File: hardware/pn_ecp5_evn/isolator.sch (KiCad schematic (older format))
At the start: 14 parts, among them U901 ADS7868, U902 ADS7868, U903 Si8640BB-B-IU, U904 Si8640BB-B-IU, U905 Si8642BB-B-IU

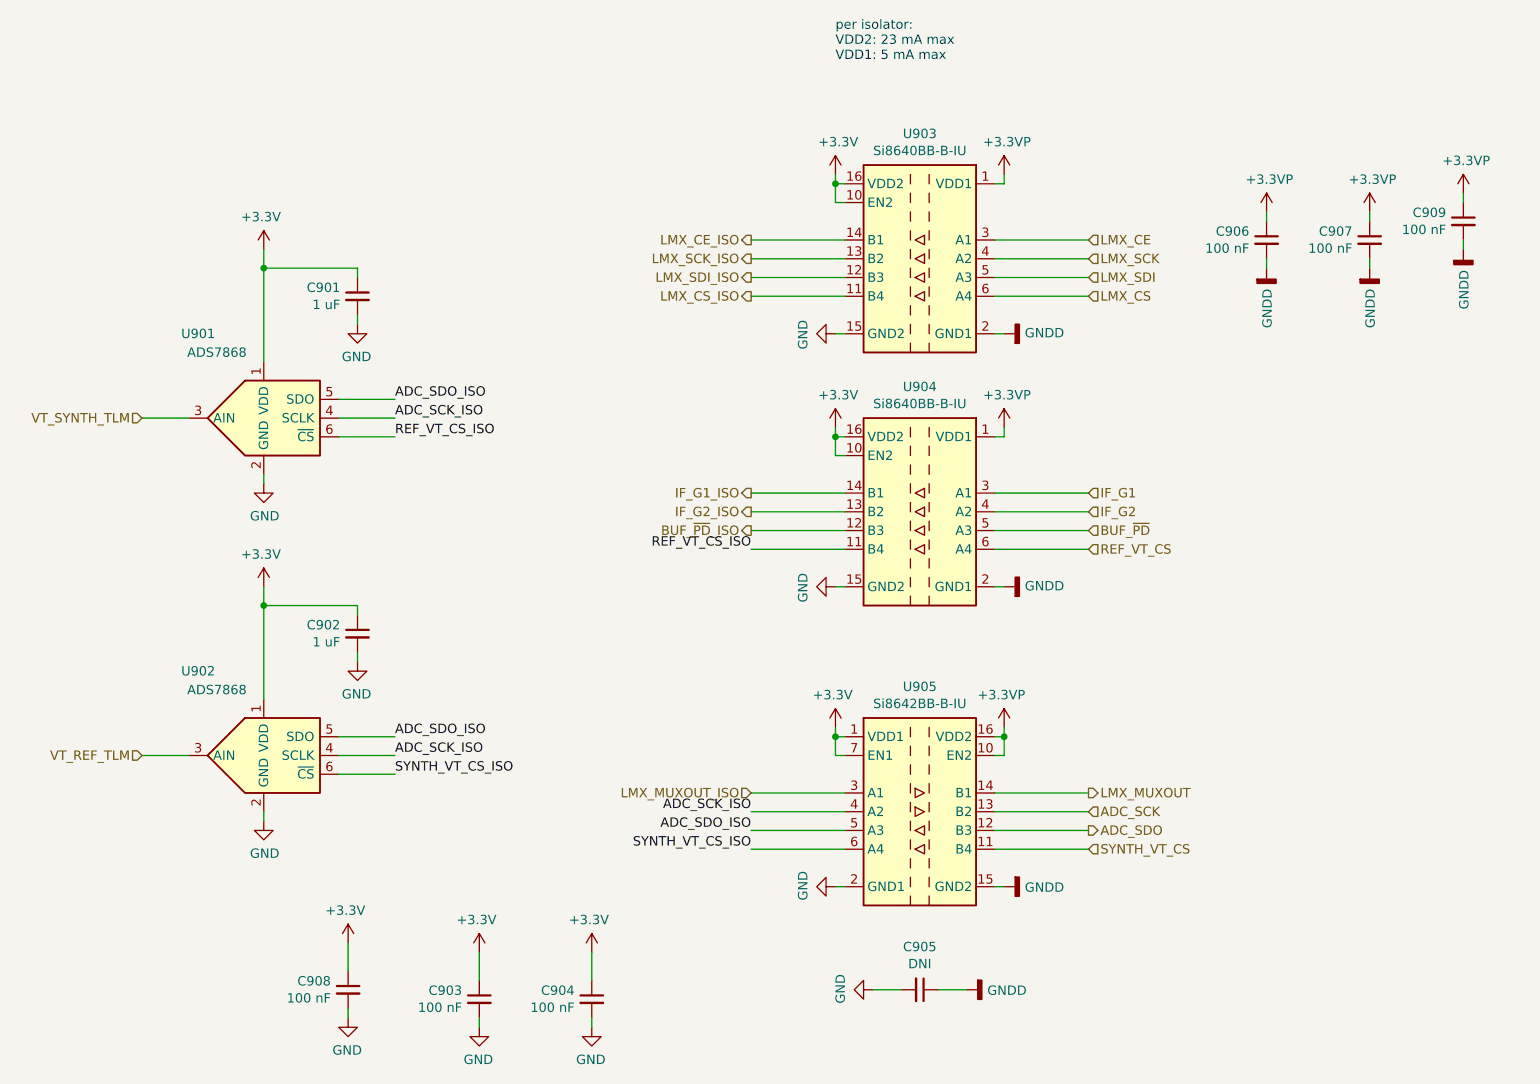
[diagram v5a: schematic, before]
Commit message: drc and erc check, schematic cleanup
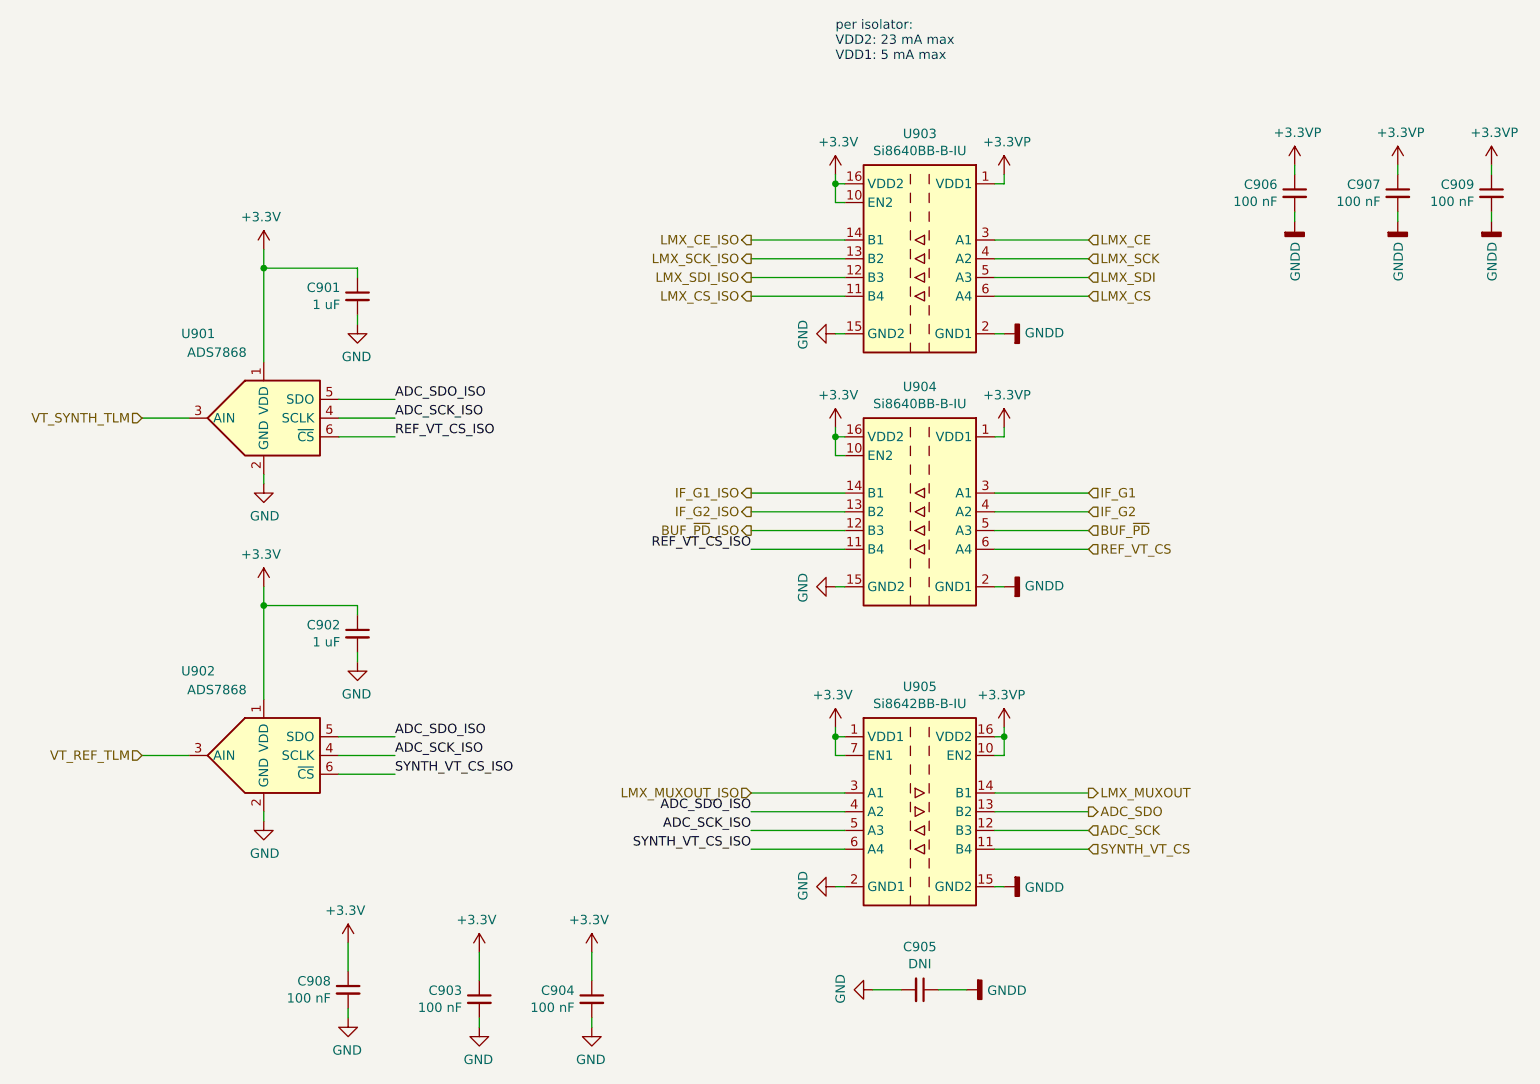
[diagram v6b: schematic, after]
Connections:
- net ADC_SCK: now also U905.12 (B3); no longer U905.13 (B2)
- net ADC_SCK_ISO: now also U905.5 (A3); no longer U905.4 (A2)
- net ADC_SDO: now also U905.13 (B2); no longer U905.12 (B3)
- net ADC_SDO_ISO: now also U905.4 (A2); no longer U905.5 (A3)
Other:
- moved on the sheet: C906, C907, C909
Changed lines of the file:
@@
 Wire Wire Line
 	4600 1950 5100 1950
+Text Label 4600 5000 2    50   ~ 0
+ADC_SCK_ISO
 Text Label 4600 4900 2    50   ~ 0
-ADC_SCK_ISO
-Text Label 4600 5000 2    50   ~ 0
 ADC_SDO_ISO
 Wire Wire Line
 	4600 4800 5100 4800
 Wire Wire Line
+	5100 4900 4600 4900
+Wire Wire Line
 	5100 5000 4600 5000
 Wire Wire Line
-	5100 4900 4600 4900
+	5900 4900 6400 4900
 Wire Wire Line
 	5900 5000 6400 5000
-Wire Wire Line
-	5900 4900 6400 4900
 Wire Wire Line
 	5900 4800 6400 4800
 Text HLabel 6400 4800 2    50   Output ~ 0
 LMX_MUXOUT
-Text HLabel 6400 4900 2    50   Input ~ 0
+Text HLabel 6400 5000 2    50   Input ~ 0
 ADC_SCK
-Text HLabel 6400 5000 2    50   Output ~ 0
+Text HLabel 6400 4900 2    50   Output ~ 0
 ADC_SDO
 $Comp
@@
 L power:+3.3VP #PWR?
 U 1 1 5F5BC2AD
-P 7350 1700
+P 7500 1450
 AR Path="/5F5BC2AD" Ref="#PWR?"  Part="1"
 AR Path="/6047B31A/5F5BC2AD" Ref="#PWR0273"  Part="1"
-F 0 "#PWR0273" H 7500 1650 50  0001 C CNN
-F 1 "+3.3VP" H 7365 1873 50  0000 C CNN
-F 2 "" H 7350 1700 50  0001 C CNN
-F 3 "" H 7350 1700 50  0001 C CNN
-	1    7350 1700
+F 0 "#PWR0273" H 7650 1400 50  0001 C CNN
+F 1 "+3.3VP" H 7515 1623 50  0000 C CNN
+F 2 "" H 7500 1450 50  0001 C CNN
+F 3 "" H 7500 1450 50  0001 C CNN
+	1    7500 1450
 	1    0    0    -1
 $EndComp
@@
 L Device:C_Small C906
 U 1 1 5F5C5982
-P 7350 1850
-F 0 "C906" H 7442 1896 50  0000 L CNN
-F 1 "100 nF" H 7442 1805 50  0000 L CNN
-F 2 "Capacitor_SMD:C_0402_1005Metric" H 7350 1850 50  0001 C CNN
-F 3 "~" H 7350 1850 50  0001 C CNN
-	1    7350 1850
+P 7500 1600
+F 0 "C906" H 7592 1646 50  0000 L CNN
+F 1 "100 nF" H 7592 1555 50  0000 L CNN
+F 2 "Capacitor_SMD:C_0402_1005Metric" H 7500 1600 50  0001 C CNN
+F 3 "~" H 7500 1600 50  0001 C CNN
+	1    7500 1600
 	-1   0    0    -1
 $EndComp
@@
 L power:GNDD #PWR?
 U 1 1 5F5C7FFB
-P 7350 2000
+P 7500 1750
 AR Path="/5F5C7FFB" Ref="#PWR?"  Part="1"
 AR Path="/6047B31A/5F5C7FFB" Ref="#PWR0274"  Part="1"
-F 0 "#PWR0274" H 7350 1750 50  0001 C CNN
-F 1 "GNDD" V 7354 1890 50  0000 R CNN
-F 2 "" H 7350 2000 50  0001 C CNN
-F 3 "" H 7350 2000 50  0001 C CNN
-	1    7350 2000
-	1    0    0    -1
-$EndComp
-Wire Wire Line
-	7350 2000 7350 1950
-Wire Wire Line
-	7350 1750 7350 1700
+F 0 "#PWR0274" H 7500 1500 50  0001 C CNN
+F 1 "GNDD" V 7504 1640 50  0000 R CNN
+F 2 "" H 7500 1750 50  0001 C CNN
+F 3 "" H 7500 1750 50  0001 C CNN
+	1    7500 1750
+	1    0    0    -1
+$EndComp
+Wire Wire Line
+	7500 1750 7500 1700
+Wire Wire Line
+	7500 1500 7500 1450
 $Comp
 L power:+3.3VP #PWR?
 U 1 1 5F5CD079
-P 7900 1700
+P 8050 1450
 AR Path="/5F5CD079" Ref="#PWR?"  Part="1"
 AR Path="/6047B31A/5F5CD079" Ref="#PWR0275"  Part="1"
-F 0 "#PWR0275" H 8050 1650 50  0001 C CNN
-F 1 "+3.3VP" H 7915 1873 50  0000 C CNN
-F 2 "" H 7900 1700 50  0001 C CNN
-F 3 "" H 7900 1700 50  0001 C CNN
-	1    7900 1700
+F 0 "#PWR0275" H 8200 1400 50  0001 C CNN
+F 1 "+3.3VP" H 8065 1623 50  0000 C CNN
+F 2 "" H 8050 1450 50  0001 C CNN
+F 3 "" H 8050 1450 50  0001 C CNN
+	1    8050 1450
 	1    0    0    -1
 $EndComp
@@
 L Device:C_Small C907
 U 1 1 5F5CD07F
-P 7900 1850
-F 0 "C907" H 7992 1896 50  0000 L CNN
-F 1 "100 nF" H 7992 1805 50  0000 L CNN
-F 2 "Capacitor_SMD:C_0402_1005Metric" H 7900 1850 50  0001 C CNN
-F 3 "~" H 7900 1850 50  0001 C CNN
-	1    7900 1850
+P 8050 1600
+F 0 "C907" H 8142 1646 50  0000 L CNN
+F 1 "100 nF" H 8142 1555 50  0000 L CNN
+F 2 "Capacitor_SMD:C_0402_1005Metric" H 8050 1600 50  0001 C CNN
+F 3 "~" H 8050 1600 50  0001 C CNN
+	1    8050 1600
 	-1   0    0    -1
 $EndComp
@@
 L power:GNDD #PWR?
 U 1 1 5F5CD085
-P 7900 2000
+P 8050 1750
 AR Path="/5F5CD085" Ref="#PWR?"  Part="1"
 AR Path="/6047B31A/5F5CD085" Ref="#PWR0276"  Part="1"
-F 0 "#PWR0276" H 7900 1750 50  0001 C CNN
-F 1 "GNDD" V 7904 1890 50  0000 R CNN
-F 2 "" H 7900 2000 50  0001 C CNN
-F 3 "" H 7900 2000 50  0001 C CNN
-	1    7900 2000
-	1    0    0    -1
-$EndComp
-Wire Wire Line
-	7900 2000 7900 1950
-Wire Wire Line
-	7900 1750 7900 1700
+F 0 "#PWR0276" H 8050 1500 50  0001 C CNN
+F 1 "GNDD" V 8054 1640 50  0000 R CNN
+F 2 "" H 8050 1750 50  0001 C CNN
+F 3 "" H 8050 1750 50  0001 C CNN
+	1    8050 1750
+	1    0    0    -1
+$EndComp
+Wire Wire Line
+	8050 1750 8050 1700
+Wire Wire Line
+	8050 1500 8050 1450
 Wire Wire Line
 	3750 6000 3750 6050
@@
 L power:+3.3VP #PWR?
 U 1 1 5F3C72BF
-P 8400 1600
+P 8550 1450
 AR Path="/5F3C72BF" Ref="#PWR?"  Part="1"
 AR Path="/6047B31A/5F3C72BF" Ref="#PWR0287"  Part="1"
-F 0 "#PWR0287" H 8550 1550 50  0001 C CNN
-F 1 "+3.3VP" H 8415 1773 50  0000 C CNN
-F 2 "" H 8400 1600 50  0001 C CNN
-F 3 "" H 8400 1600 50  0001 C CNN
-	1    8400 1600
+F 0 "#PWR0287" H 8700 1400 50  0001 C CNN
+F 1 "+3.3VP" H 8565 1623 50  0000 C CNN
+F 2 "" H 8550 1450 50  0001 C CNN
+F 3 "" H 8550 1450 50  0001 C CNN
+	1    8550 1450
 	1    0    0    -1
 $EndComp
@@
 L Device:C_Small C909
 U 1 1 5F3C72C5
-P 8400 1750
-F 0 "C909" H 8492 1796 50  0000 L CNN
-F 1 "100 nF" H 8492 1705 50  0000 L CNN
-F 2 "Capacitor_SMD:C_0402_1005Metric" H 8400 1750 50  0001 C CNN
-F 3 "~" H 8400 1750 50  0001 C CNN
-	1    8400 1750
+P 8550 1600
+F 0 "C909" H 8642 1646 50  0000 L CNN
+F 1 "100 nF" H 8642 1555 50  0000 L CNN
+F 2 "Capacitor_SMD:C_0402_1005Metric" H 8550 1600 50  0001 C CNN
+F 3 "~" H 8550 1600 50  0001 C CNN
+	1    8550 1600
 	-1   0    0    -1
 $EndComp
@@
 L power:GNDD #PWR?
 U 1 1 5F3C72CB
-P 8400 1900
+P 8550 1750
 AR Path="/5F3C72CB" Ref="#PWR?"  Part="1"
 AR Path="/6047B31A/5F3C72CB" Ref="#PWR0288"  Part="1"
-F 0 "#PWR0288" H 8400 1650 50  0001 C CNN
-F 1 "GNDD" V 8404 1790 50  0000 R CNN
-F 2 "" H 8400 1900 50  0001 C CNN
-F 3 "" H 8400 1900 50  0001 C CNN
-	1    8400 1900
-	1    0    0    -1
-$EndComp
-Wire Wire Line
-	8400 1900 8400 1850
-Wire Wire Line
-	8400 1650 8400 1600
+F 0 "#PWR0288" H 8550 1500 50  0001 C CNN
+F 1 "GNDD" V 8554 1640 50  0000 R CNN
+F 2 "" H 8550 1750 50  0001 C CNN
+F 3 "" H 8550 1750 50  0001 C CNN
+	1    8550 1750
+	1    0    0    -1
+$EndComp
+Wire Wire Line
+	8550 1750 8550 1700
+Wire Wire Line
+	8550 1500 8550 1450
 Text HLabel 6400 3400 2    50   Input ~ 0
 BUF_~PD

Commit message: added part numbers to schematic of phase noise downconverter, ordered
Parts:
- C901, C902, C903, C904, C905, C906, C907, C908, C909: Distributor Part Number (none) -> N/A
- U901, U902: Distributor (none) -> Digi-Key; Distributor Part Number (none) -> 296-41406-1-ND
- U903, U904: Distributor (none) -> Mouser; Distributor Part Number (none) -> 634-SI8640BB-B-IU
- U905: Distributor (none) -> Mouser; Distributor Part Number (none) -> 634-SI8642BB-B-IU
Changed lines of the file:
@@
 F 2 "Package_SO:QSOP-16_3.9x4.9mm_P0.635mm" H 5500 1400 50  0001 C CIN
 F 3 "https://www.silabs.com/documents/public/data-sheets/si864x-datasheet.pdf" H 5500 2350 50  0001 C CNN
+F 4 "Mouser" H 5500 1950 50  0001 C CNN "Distributor"
+F 5 "634-SI8640BB-B-IU " H 5500 1950 50  0001 C CNN "Distributor Part Number"
 	1    5500 1950
 	-1   0    0    -1
@@
 F 2 "Package_SO:QSOP-16_3.9x4.9mm_P0.635mm" H 5500 2750 50  0001 C CIN
 F 3 "https://www.silabs.com/documents/public/data-sheets/si864x-datasheet.pdf" H 5500 3700 50  0001 C CNN
+F 4 "Mouser" H 5500 3300 50  0001 C CNN "Distributor"
+F 5 "634-SI8640BB-B-IU " H 5500 3300 50  0001 C CNN "Distributor Part Number"
 	1    5500 3300
 	-1   0    0    -1
@@
 F 2 "Package_TO_SOT_SMD:TSOT-23-6" H 2000 4550 50  0001 C CNN
 F 3 "http://www.ti.com/lit/ds/symlink/ads7866.pdf" H 2050 4850 50  0001 C CNN
+F 4 "Digi-Key" H 2000 4600 50  0001 C CNN "Distributor"
+F 5 " 296-41406-1-ND" H 2000 4600 50  0001 C CNN "Distributor Part Number"
 	1    2000 4600
 	1    0    0    -1
@@
 F 2 "Capacitor_SMD:C_0402_1005Metric" H 2500 3950 50  0001 C CNN
 F 3 "~" H 2500 3950 50  0001 C CNN
+F 4 "N/A" H 2500 3950 50  0001 C CNN "Distributor Part Number"
 	1    2500 3950
 	-1   0    0    -1
@@
 F 2 "Package_TO_SOT_SMD:TSOT-23-6" H 2000 2750 50  0001 C CNN
 F 3 "http://www.ti.com/lit/ds/symlink/ads7866.pdf" H 2050 3050 50  0001 C CNN
+F 4 "Digi-Key" H 2000 2800 50  0001 C CNN "Distributor"
+F 5 " 296-41406-1-ND" H 2000 2800 50  0001 C CNN "Distributor Part Number"
 	1    2000 2800
 	1    0    0    -1
@@
 F 2 "Capacitor_SMD:C_0402_1005Metric" H 2500 2150 50  0001 C CNN
 F 3 "~" H 2500 2150 50  0001 C CNN
+F 4 "N/A" H 2500 2150 50  0001 C CNN "Distributor Part Number"
 	1    2500 2150
 	-1   0    0    -1
@@
 F 2 "Package_SO:QSOP-16_3.9x4.9mm_P0.635mm" H 5500 4350 50  0001 C CIN
 F 3 "https://www.silabs.com/documents/public/data-sheets/si864x-datasheet.pdf" H 5500 5300 50  0001 C CNN
+F 4 "Mouser" H 5500 4900 50  0001 C CNN "Distributor"
+F 5 "634-SI8642BB-B-IU" H 5500 4900 50  0001 C CNN "Distributor Part Number"
 	1    5500 4900
 	1    0    0    -1
@@
 F 2 "Capacitor_SMD:C_0402_1005Metric" H 5500 5850 50  0001 C CNN
 F 3 "~" H 5500 5850 50  0001 C CNN
+F 4 "N/A" H 5500 5850 50  0001 C CNN "Distributor Part Number"
 	1    5500 5850
 	0    1    1    0
@@
 F 2 "Capacitor_SMD:C_0402_1005Metric" H 7500 1600 50  0001 C CNN
 F 3 "~" H 7500 1600 50  0001 C CNN
+F 4 "N/A" H 7500 1600 50  0001 C CNN "Distributor Part Number"
 	1    7500 1600
 	-1   0    0    -1
@@
 F 2 "Capacitor_SMD:C_0402_1005Metric" H 8050 1600 50  0001 C CNN
 F 3 "~" H 8050 1600 50  0001 C CNN
+F 4 "N/A" H 8050 1600 50  0001 C CNN "Distributor Part Number"
 	1    8050 1600
 	-1   0    0    -1
@@
 F 2 "Capacitor_SMD:C_0402_1005Metric" H 3750 5900 50  0001 C CNN
 F 3 "~" H 3750 5900 50  0001 C CNN
+F 4 "N/A" H 3750 5900 50  0001 C CNN "Distributor Part Number"
 	1    3750 5900
 	-1   0    0    -1
@@
 F 2 "Capacitor_SMD:C_0402_1005Metric" H 3150 5900 50  0001 C CNN
 F 3 "~" H 3150 5900 50  0001 C CNN
+F 4 "N/A" H 3150 5900 50  0001 C CNN "Distributor Part Number"
 	1    3150 5900
 	-1   0    0    -1
@@
 F 2 "Capacitor_SMD:C_0402_1005Metric" H 2450 5850 50  0001 C CNN
 F 3 "~" H 2450 5850 50  0001 C CNN
+F 4 "N/A" H 2450 5850 50  0001 C CNN "Distributor Part Number"
 	1    2450 5850
 	-1   0    0    -1
@@
 F 2 "Capacitor_SMD:C_0402_1005Metric" H 8550 1600 50  0001 C CNN
 F 3 "~" H 8550 1600 50  0001 C CNN
+F 4 "N/A" H 8550 1600 50  0001 C CNN "Distributor Part Number"
 	1    8550 1600
 	-1   0    0    -1
